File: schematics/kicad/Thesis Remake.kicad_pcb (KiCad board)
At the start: 2 copper layers, 73 x 73 mm, 112 parts, among them J1 SJ2-35853B-SMT-TR, J2 Conn_01x18, J3 Conn_01x18, J4 Conn_01x01_Pin, J5 Conn_01x01_Pin, J6 Conn_01x01_Pin, J7 Conn_01x01_Pin, U1 CD4051B, U10 MCP6001-OT, U11 MCP6001-OT, U2 PCM5102, U5 RT9080-33GJ5, U6 LM2940CT-5.0_MOD, U7 TPA711, U8 LM2940CT-5.0_MOD, U9 MCP6001-OT

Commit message: Commits
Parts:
- removed 0V1: TestPoint, TestPoint:TestPoint_Pad_1.5x1.5mm
- removed C_COUPLING_MUX1: 10nF, Capacitor_SMD:C_1206_3216Metric_Pad1.33x1.80mm_HandSolder
- removed D3: D_Schottky, Diode_SMD:D_SOD-123F
- removed JP1, JP2, JP4, JP5, JP6, JP7, JP8, JP9: Jumper_2_Open, Jumper:SolderJumper-2_P1.3mm_Open_Pad1.0x1.5mm
- removed R_COUPLING_AMPSTAGE2: 10K, Resistor_SMD:R_0805_2012Metric_Pad1.20x1.40mm_HandSolder
- removed R_COUPLING_AMPSTAGE3: 1K, Resistor_SMD:R_0805_2012Metric_Pad1.20x1.40mm_HandSolder
- removed R_LADDER_4, R_LADDER_5, R_LADDER_6, R_LADDER_7, R_LADDER_8: 1k, Resistor_SMD:R_0805_2012Metric_Pad1.20x1.40mm_HandSolder
- removed U1: CD4051B, Package_SO:SOIC-16_3.9x9.9mm_P1.27mm
- added C_COUPLING_MUX2: 10nF, Capacitor_SMD:C_1206_3216Metric_Pad1.33x1.80mm_HandSolder, F.Cu at (231.7, 66.3)
- added Q1: MMBT7002K, Package_TO_SOT_SMD:SOT-23, F.Cu at (228.1, 71.4)
- added RG3: 470, Resistor_SMD:R_0805_2012Metric_Pad1.20x1.40mm_HandSolder, F.Cu at (224.9, 71.3)
- added RL1: 5K, Resistor_SMD:R_0805_2012Metric_Pad1.20x1.40mm_HandSolder, F.Cu at (228.1, 67.2)
- added S2: B3F-1000, B3F-1000:SW_B3F-1000, F.Cu at (263.0, 56.9)
- added U3: SN74LVC1G3157, Package_TO_SOT_SMD:SOT-23-6, F.Cu at (231.7, 71.2)
- C_INPUT_TPA2: value 100nF -> 0.1uF
- moved S1 5.95 mm to (254.7, 56.8), turned to -90 degrees
- moved D5 5.56 mm to (213.0, 42.8), turned to 180 degrees
- moved JP3 3.07 mm to (254.1, 97.5)
- moved D7 2.77 mm to (263.9, 50.5)
- moved D8 2.77 mm to (263.9, 47.3)
- moved D9 2.77 mm to (263.8, 44.0)
- moved R5 2.77 mm to (267.4, 50.5)
- moved R6 2.77 mm to (267.4, 47.3)
- moved R7 2.77 mm to (267.4, 44.0)
- moved TP_Vo+_TPA1 2.45 mm to (252.2, 72.4)
- moved TP_VDD_TPA1 2.24 mm to (258.7, 67.9)
- moved CB_TPA1 2.11 mm to (238.5, 65.1), turned to 90 degrees
- moved OUTPUT_AS1 1.33 mm to (259.0, 97.6)
- moved TP_Vo-_TPA1 0.87 mm to (254.7, 63.9)
- moved R_LADDER_2 0.51 mm to (205.4, 59.4)
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- renumbered BCK1 to BCK, DIN1 to DIN, LRCK1 to LRCK, VDD1 to VDD
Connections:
- C_GND_AMPSTAGE3 pad 1: /OUTDACR -> /Filter
- C_INPUT_LDO2 pad 2: Net-(D3-K) -> +15V_Diode
- C_INPUT_LDO3 pad 2: Net-(D5-K) -> +15V_Diode
- C_IN_+15V_2 pad 1: Net-(D3-K) -> +15V_Diode
- C_IN_+15V_3 pad 1: Net-(D5-K) -> +15V_Diode
- D5 pad 1: Net-(D5-K) -> +15V_Diode
- J2 pad 17: unconnected-(J2-Pin_17-Pad17) -> +3v3_ESP
- J2 pad 2: unconnected-(J2-Pin_2-Pad2) -> /Poll_Button_2
- J2 pad 3: /Poll Button -> /Poll_Button_1
- J3 pad 1: /ADC -> unconnected-(J3-Pin_1-Pad1)
- J3 pad 5: unconnected-(J3-Pin_5-Pad5) -> /ADC
- R_LADDER_2 pad 1: +4.375V -> /ADC
- R_LADDER_2 pad 2: +5V1 -> +3v3_ESP
- R_LADDER_3 pad 1: +3.75V -> /ADC
- R_LADDER_3 pad 2: +4.375V -> GND
- S1 pad 1: /Poll Button -> GND
- S1 pad 2: GND -> unconnected-(S1-Pad2)
- S1 pad 3: GND -> unconnected-(S1-Pad3)
- S1 pad 4: /Poll Button -> /Poll_Button_1
- U6 pad 1: Net-(D3-K) -> +15V_Diode
- U8 pad 1: Net-(D5-K) -> +15V_Diode
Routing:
- net /Filter_IN: track 69.0 -> 11.5 mm, vias 2 -> 0
- net GND: track 29.3 -> 85.6 mm, vias 5 -> 56
- net /Poll Button: track 44.5 -> 0.00 mm
- net +15V_Diode: track 0.00 -> 22.3 mm
- net /Poll_Button_2: track 0.00 -> 20.6 mm
- net /Filter: track 0.00 -> 19.6 mm
- net /Poll_Button_1: track 0.00 -> 14.8 mm
- net /OUTDACR: track 40.9 -> 28.4 mm, vias 0 -> 2
- net +15V: track 17.4 -> 5.53 mm
- net +5V: track 212.1 -> 222.7 mm, vias 6 -> 8
- net Net-(D3-K): track 7.60 -> 0.00 mm
- net Net-(D5-K): track 7.60 -> 0.00 mm
- net Net-(JP3-A): track 14.9 -> 7.43 mm
- net +4.375V: track 7.39 -> 0.00 mm
- net +3.75V: track 7.37 -> 0.00 mm
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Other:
- board text removed: "1 2 3 4 5 6 7 8"

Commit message: Commits
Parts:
- D7, D8, D9: footprint LED_THT:LED_D2.0mm_W4.8mm_H2.5mm_FlatTop -> LED_SMD:LED_0805_2012Metric_Pad1.15x1.40mm_HandSolder
- moved D7 1.03 mm to (262.9, 50.6)
- moved D9 1.01 mm to (262.8, 44.0)
- moved D8 0.99 mm to (262.9, 47.3)
- renumbered BCK to BCK1, DIN to DIN1, LRCK to LRCK1, VDD to VDD1
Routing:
- net /LED_2: track 39.9 -> 40.5 mm
- net /LED_3: track 43.6 -> 44.1 mm

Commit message: Commits
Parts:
- renumbered BCK1 to BCK, DIN1 to DIN, LRCK1 to LRCK
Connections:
- CI_TPA711 pad 2: /BUFFEROUT -> /Bypass
- C_GND_AMPSTAGE3 pad 1: /Filter -> /OUTDACR
- U3 pad 1: /Filter -> /BUFFEROUT
- U3 pad 3: /BUFFEROUT -> /OUTDACR
- U3 pad 4: /OUTDACR -> /Bypass
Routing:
- net /Filter: track 19.6 -> 0.00 mm
- net /Bypass: track 0.00 -> 7.96 mm
- net /OUTDACR: track 28.4 -> 31.7 mm
- net /BUFFEROUT: track 49.8 -> 49.1 mm, vias 0 -> 2
- net GND: vias 56 -> 54

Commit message: code commits
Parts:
- removed C_COUPLING_AMPSTAGE4: 10nF, Capacitor_SMD:C_1206_3216Metric_Pad1.33x1.80mm_HandSolder
- removed C_INPUT_LDO2: 0.47uF, Capacitor_SMD:C_1206_3216Metric_Pad1.33x1.80mm_HandSolder
- removed C_INPUT_RT1, C_OUTPUT_LDO2: 22uF, Capacitor_SMD:C_1206_3216Metric_Pad1.33x1.80mm_HandSolder
- removed C_IN_+15V_2: 10uF, Capacitor_SMD:C_1206_3216Metric_Pad1.33x1.80mm_HandSolder
- removed STATUS_LED2: 330, Resistor_SMD:R_0805_2012Metric_Pad1.20x1.40mm_HandSolder
- added C23: 10nF, Capacitor_SMD:C_1206_3216Metric_Pad1.33x1.80mm_HandSolder, F.Cu at (253.9, 38.5)
- added C4: 10uF, Capacitor_SMD:C_1206_3216Metric_Pad1.33x1.80mm_HandSolder, F.Cu at (216.7, 47.5)
- added C5: 0.47uF, Capacitor_SMD:C_1206_3216Metric_Pad1.33x1.80mm_HandSolder, F.Cu at (219.1, 47.5)
- added C6: 22uF, Capacitor_SMD:C_1206_3216Metric_Pad1.33x1.80mm_HandSolder, F.Cu at (228.9, 47.6)
- added C8: 22uF, Capacitor_SMD:C_1206_3216Metric_Pad1.33x1.80mm_HandSolder, F.Cu at (210.9, 86.5)
- added R2: 330, Resistor_SMD:R_0805_2012Metric_Pad1.20x1.40mm_HandSolder, F.Cu at (233.7, 45.8)
- renumbered BCK to BCK1, C_IN_+15V_3 to C1, CG2_PCM5102 to C10, C1_APS_PCM5102 to C11, C2_APS_PCM5102 to C12, C1_CPPS_PCM1 to C13, C2_CPPS_PCM1 to C14, C1_DPS_PCM1 to C15, C2_DPS_PCM1 to C16, C_GND_AMPSTAGE3 to C17, C_COUPLING_AMPSTAGE2 to C18, C_COUPLING_AMPSTAGE1 to C19, C_INPUT_LDO3 to C2, C_GND_AMPSTAGE1 to C20, C_IN_AMPSTAGE1 to C21, C_COUPLING_AMPSTAGE3 to C22, C_GND_AMPSTAGE2 to C24, CB_TPA1 to C25, C_SE/BTL_TPA1 to C26, C_INPUT_TPA1 to C27, C_INPUT_TPA2 to C28, CF_TPA711 to C29, C_OUTPUT_LDO3 to C3, C_INPUT_TPA3 to C30, C_COUPLING_MUX2 to C31, CA_PCM5102 to C32, CI_TPA711 to C33, C_INPUT_RT9080 to C7, CG1_PCM5102 to C9, DIN to DIN1, LRCK to LRCK1, STATUS_LED3 to R1, R3 to R10, R4 to R11, RG2 to R12, RF2 to R13, R13 to R14, R12 to R15, RF_TPA711 to R16, RI_TPA711 to R17, R11 to R18, RL1 to R19, RG3 to R20, R_LADDER_2 to R21, R_LADDER_3 to R22, R5 to R23, R6 to R24, R7 to R25, ROUTDACL1 to R3, ROUTDACR1 to R4, R1 to R5, R2 to R6, RG1 to R7, RF1 to R8, R_COUPLING_AMPSTAGE1 to R9

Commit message: QOL PCB changes
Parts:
- removed OUT_DAC_L1: TestPoint, TestPoint:TestPoint_Pad_1.5x1.5mm
- moved Vo+1 8.44 mm to (260.6, 72.4)
- moved Vo-1 6.03 mm to (260.7, 64.5)
- moved S2 4.57 mm to (267.6, 57.0)
- moved S1 3.90 mm to (258.6, 57.0)
- moved LS1 2.84 mm to (268.9, 67.9)
- moved R18 1.44 mm to (260.4, 75.6)
- moved BCK1 1.00 mm to (202.8, 68.7)
- moved C30 0.97 mm to (263.6, 74.1), turned to -90 degrees
- moved DIN1 0.71 mm to (202.8, 72.5)
- moved OUT_DAC_R1 0.61 mm to (233.4, 86.9)
- moved C10 0.61 mm to (235.0, 89.4)
- moved C9 0.61 mm to (235.0, 91.9)
- moved R3 0.61 mm to (230.5, 91.7)
- moved R4 0.61 mm to (230.5, 89.6)
- renumbered TP_Vo+_TPA1 to Vo+1, TP_Vo-_TPA1 to Vo-1
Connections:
- J2 pad 2: /Poll_Button_2 -> unconnected-(J2-Pin_2-Pad2)
- J2 pad 3: /Poll_Button_1 -> /Poll_Button_2
- J2 pad 4: /HI_LO -> /Poll_Button_1
- J2 pad 5: unconnected-(J2-Pin_5-Pad5) -> /HI_LO
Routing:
- net /Poll_Button_2: track 20.6 -> 26.9 mm
- net /Poll_Button_1: track 14.8 -> 20.4 mm
- net /Vo+: track 34.6 -> 30.1 mm
- net /HI_LO: track 24.5 -> 20.2 mm
- net +5V: track 222.7 -> 220.2 mm
- net /OUTDACL: track 4.59 -> 2.06 mm
- net /Filter_OUT: track 31.6 -> 29.5 mm
- net GND: track 85.6 -> 87.3 mm, vias 54 -> 56
- net /Vo-: track 24.3 -> 25.3 mm
- net Net-(C30-Pad2): track 19.3 -> 18.4 mm
- net /LED_2: track 40.5 -> 39.8 mm, vias 2 -> 1
- net /BUFFEROUT: track 49.1 -> 49.7 mm
- net /ADC: track 38.7 -> 39.2 mm
- net /LED_3: track 44.1 -> 43.7 mm, vias 2 -> 1
- net /LED_1: track 36.4 -> 36.3 mm, vias 2 -> 1
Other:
- board text added: "+15V"
- board text added: "FILTER_IN"
- board text added: "FILTER_OUT"
- board text added: "GND"

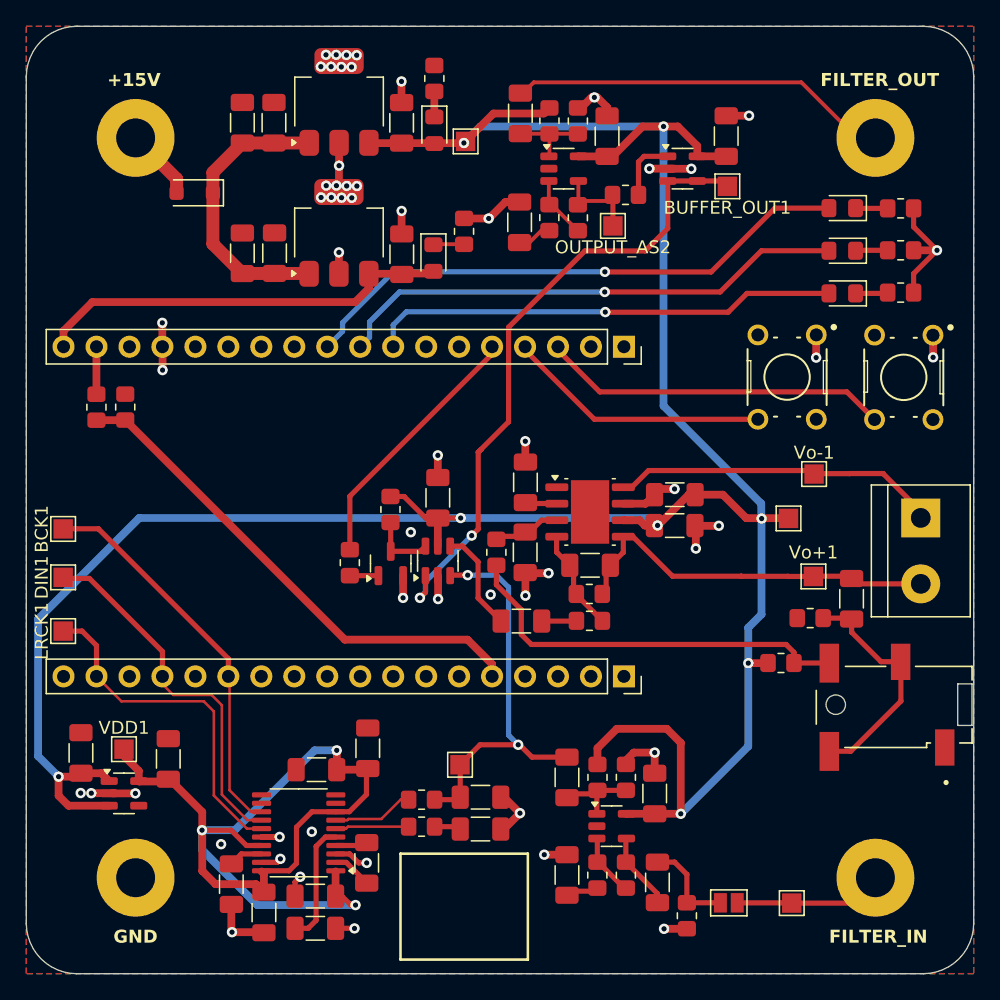
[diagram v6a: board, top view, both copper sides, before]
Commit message: LUT Works now.
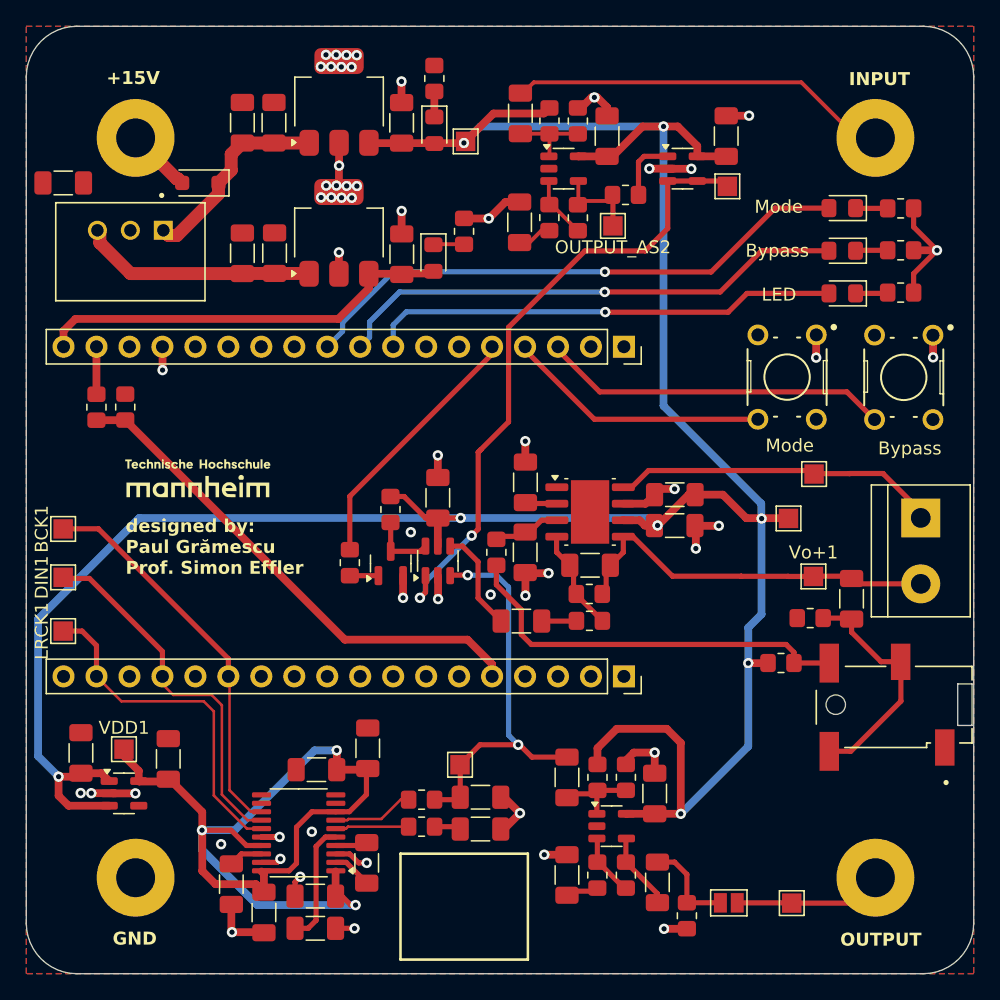
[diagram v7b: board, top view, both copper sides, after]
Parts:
- added C34: 10uF, Capacitor_SMD:C_1206_3216Metric_Pad1.33x1.80mm_HandSolder, F.Cu at (202.8, 42.1)
- added G***: LOGO, TH_MA_LOGO:TH_MA_Logo, F.Cu at (213.2, 64.8)
- added PS1: TSR_0.5-2465, TSR_0.5-2465:CONV_TSR_0.5-2465, F.Cu at (208.0, 47.4)
- moved D5 0.87 mm to (213.4, 42.1)
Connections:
- C4 pad 1: +15V_Diode -> +6.5V
- C5 pad 2: +15V_Diode -> +6.5V
- U6 pad 1: +15V_Diode -> +6.5V
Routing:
- net +6.5V: track 0.00 -> 18.3 mm
- net +15V_Diode: track 22.3 -> 15.6 mm
- net GND: track 87.3 -> 85.6 mm, vias 56 -> 55
- net +15V: track 5.53 -> 5.02 mm
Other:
- board text added: "Bypass"
- board text added: "INPUT"
- board text added: "LED"
- board text added: "Mode"
- board text added: "OUTPUT"
- board text added: "designed by: Paul Grămescu Prof. Simon Effler"
- board text removed: "FILTER_IN"
- board text removed: "FILTER_OUT"

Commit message: Commits
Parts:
- Vo-1: footprint TestPoint:TestPoint_Pad_1.5x1.5mm -> TestPoint:TestPoint_Pad_2.5x2.5mm
- moved Vo-1 2.10 mm to (262.6, 65.4)
- moved C34 1.56 mm to (202.9, 40.5), turned to 90 degrees
- moved PS1 0.83 mm to (208.8, 47.6)
- moved LS1 0.83 mm to (268.9, 68.7)
- moved D5 0.52 mm to (213.9, 42.0)
- moved G*** 0.19 mm to (213.0, 64.9)
- moved D7 0.06 mm to (262.9, 50.5)
- renumbered BCK1 to BCK, DIN1 to DIN, LRCK1 to LRCK
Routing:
- net +15V_Diode: track 15.6 -> 26.0 mm
- net /Vo-: track 25.3 -> 26.4 mm
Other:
- board text added: "No:"
